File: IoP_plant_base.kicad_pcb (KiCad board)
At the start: 2 copper layers, 51.6 x 53.1 mm, 47 parts, among them IC1 HX711, J1 Conn_01x02, J2 Jack-DC, J3 Conn_01x02, J4 Conn_01x02, J5 Conn_01x03, J6 Conn_01x02, J7 Conn_01x05, Q1 BC857C, U1 NodeMCUv2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

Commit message: Started routing boost converter. TODO: footprint name fixing.
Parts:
- moved R3 57.7 mm to (114.4, 77.7)
- moved R2 57.5 mm to (115.9, 83.4)
- moved C4 52.6 mm to (114.3, 80.0), turned to 180 degrees
- moved R1 52.3 mm to (119.5, 83.2), turned to 180 degrees
- moved C3 50.1 mm to (122.8, 82.7), turned to 90 degrees
- moved C5 47.1 mm to (119.7, 74.4), turned to 270 degrees
- moved D2 43.0 mm to (124.1, 76.3), turned to 270 degrees
- moved U2 39.3 mm to (119.7, 79.0)
- moved J4 37.6 mm to (100.4, 82.3), turned to 90 degrees
- moved L1 35.5 mm to (126.2, 82.4)
- moved D1 30.4 mm to (140.1, 77.5)
- moved C2 28.1 mm to (134.9, 82.9)
- moved F1 27.3 mm to (134.8, 77.8)
- moved C1 27.2 mm to (134.9, 80.6)
- moved J3 25.5 mm to (103.9, 90.0), turned to 180 degrees
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
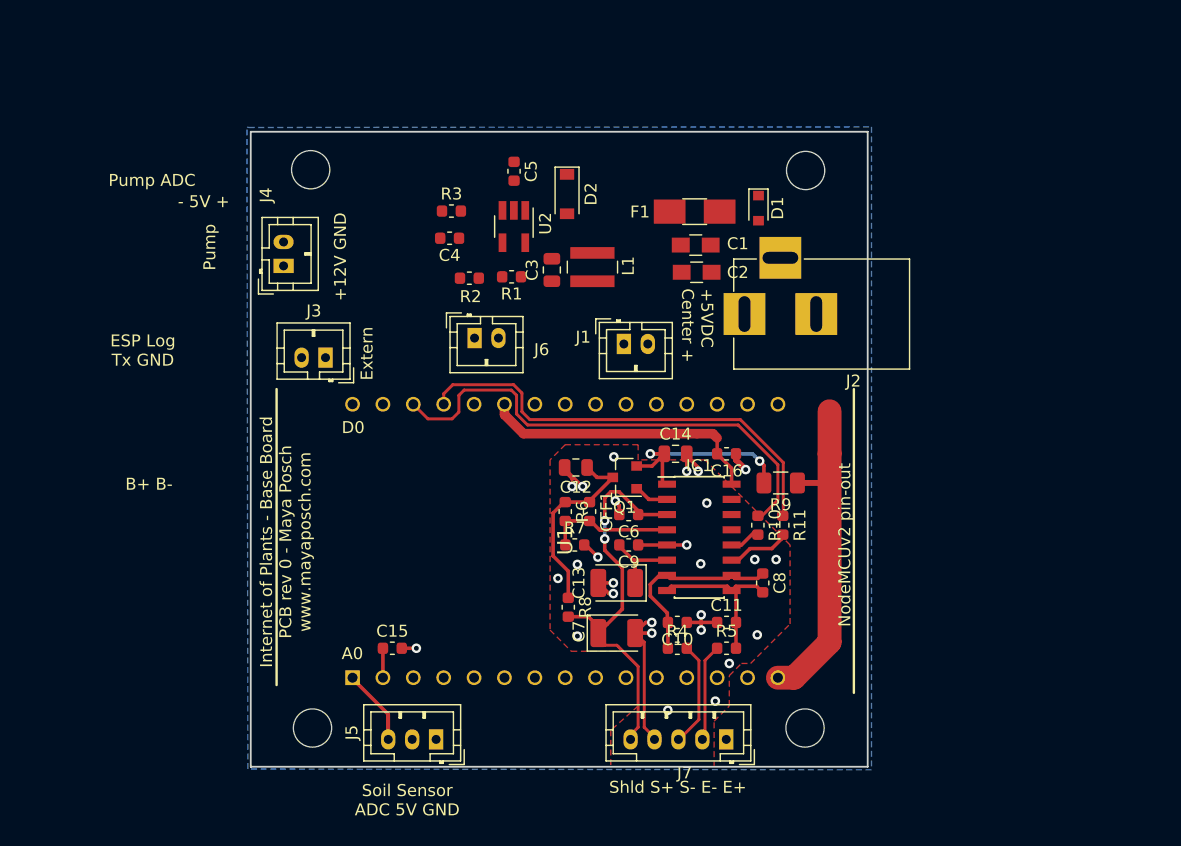
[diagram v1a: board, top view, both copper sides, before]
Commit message: Finish initial PCB routing.
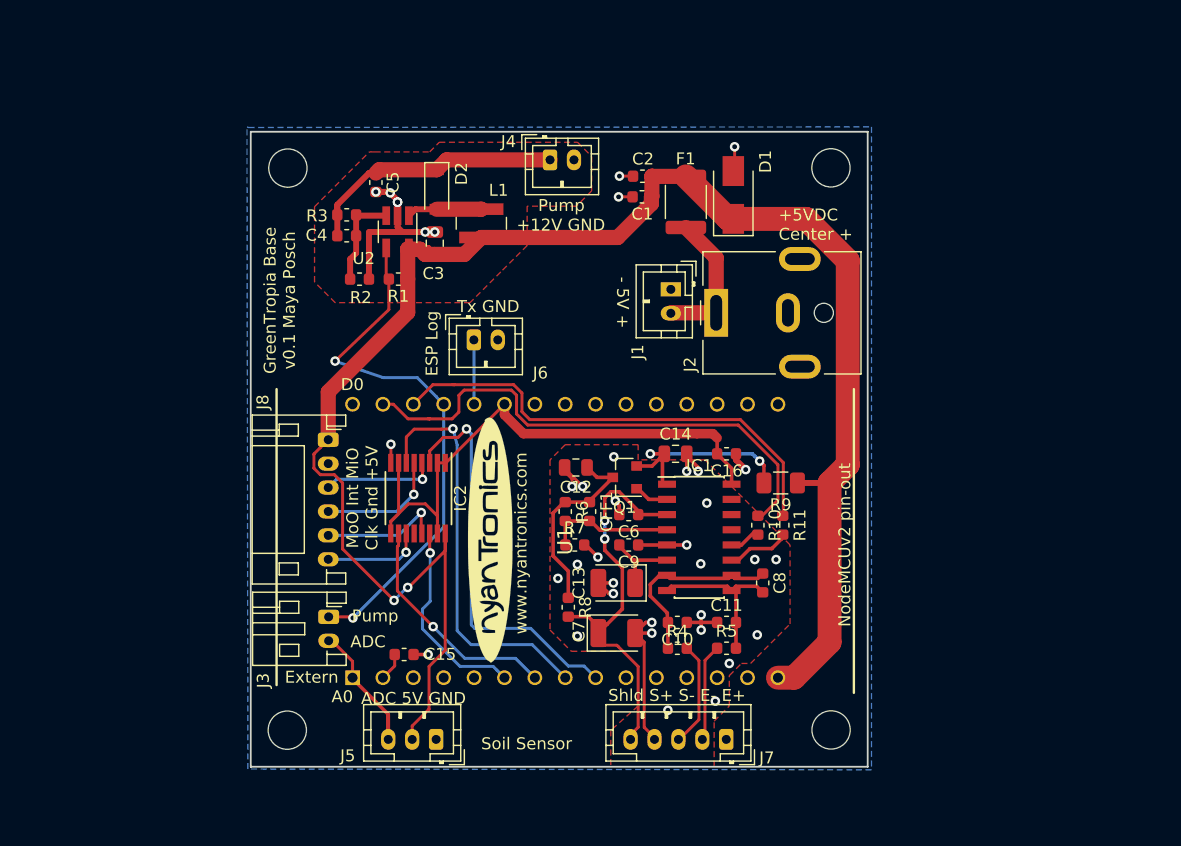
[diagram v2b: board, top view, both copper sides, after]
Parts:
- removed REF** (x4): MountingHole_3.2mm_M3_DIN965, Mounting_Holes:MountingHole_3.2mm_M3_DIN965
- added G***: LOGO, kicad_art:nyantronics_logo, F.Cu at (117.6, 105.3)
- added H1: MountingHole, MountingHole:MountingHole_3.2mm_M3_DIN965, F.Cu at (146.2, 121.1)
- added H2: MountingHole, MountingHole:MountingHole_3.2mm_M3_DIN965, F.Cu at (146.2, 74.1)
- added H3: MountingHole, MountingHole:MountingHole_3.2mm_M3_DIN965, F.Cu at (100.7, 121.1)
- added H4: MountingHole, MountingHole:MountingHole_3.2mm_M3_DIN965, F.Cu at (100.8, 74.2)
- added IC2: CD40109BPW, Package_SO:TSSOP-16_4.4x5mm_P0.65mm, F.Cu at (111.6, 101.8)
- added J8: Conn_01x06, Connector_JST:JST_PH_S6B-PH-K_1x06_P2.00mm_Horizontal, F.Cu at (104.1, 96.9)
- C1, C2: footprint Capacitors_SMD:C_0805_HandSoldering -> Capacitor_SMD:C_0603_1608Metric
- D1: footprint Diodes_SMD:D_0805 -> Diode_SMD:D_SMA
- F1: footprint Fuse_Holders_and_Fuses:Fuse_SMD1206_HandSoldering -> Fuse:Fuse_1812_4532Metric
- J2: footprint Connectors:BARREL_JACK -> Connector_BarrelJack:BarrelJack_CUI_PJ-063AH_Horizontal
- J3: footprint Connectors_JST:JST_PH_B2B-PH-K_02x2.00mm_Straight -> Connector_JST:JST_PH_S2B-PH-K_1x02_P2.00mm_Horizontal
- J4, J6: footprint Connectors_JST:JST_PH_B2B-PH-K_02x2.00mm_Straight -> Connector_JST:JST_PH_B2B-PH-K_1x02_P2.00mm_Vertical
- J5: footprint Connectors_JST:JST_PH_B3B-PH-K_03x2.00mm_Straight -> Connector_JST:JST_PH_B3B-PH-K_1x03_P2.00mm_Vertical
- J7: footprint Connectors_JST:JST_PH_B5B-PH-K_05x2.00mm_Straight -> Connector_JST:JST_PH_B5B-PH-K_1x05_P2.00mm_Vertical
- moved J4 24.0 mm to (122.7, 73.5), turned to 0 degrees
- moved J3 21.7 mm to (104.2, 111.7), turned to 270 degrees
- moved C5 11.6 mm to (108.1, 75.4)
- moved D2 10.9 mm to (113.2, 75.9)
- moved C3 10.0 mm to (113.0, 80.4)
- moved L1 9.98 mm to (116.9, 78.8)
- moved U2 9.73 mm to (109.9, 79.5)
- moved R1 9.47 mm to (110.0, 83.4)
- moved C2 9.22 mm to (130.4, 74.8), turned to 180 degrees
- moved R2 9.18 mm to (106.8, 83.4)
- moved R3 8.76 mm to (105.7, 78.1)
- moved C4 8.61 mm to (105.7, 79.8)
- moved C1 6.04 mm to (130.4, 76.6), turned to 180 degrees
- moved J1 6.02 mm to (132.8, 84.3), turned to 270 degrees
- moved D1 2.37 mm to (138.0, 76.4), turned to 90 degrees
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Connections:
- net Net-(J6-Pad1) renamed /Dbg
- U1 pad 27: SCL_CLK -> PUMP_EN
- U1 pad 28: SCL_DOUT -> SCL_CLK
- U1 pad 29: PUMP_EN -> SCL_DOUT
- U1 pad 6: Net-(U1-Pad6) -> SPI_INT
- U1 pad 7: Net-(U1-Pad7) -> SPI_MOSI
- U1 pad 8: Net-(U1-Pad8) -> SPI_MISO
- U1 pad 9: Net-(U1-Pad9) -> SPI_CLK
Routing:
- net +5VDC: track 27.5 -> 149.1 mm, vias 0 -> 2
- net PUMP_EN: track 0.00 -> 44.9 mm, vias 0 -> 2
- net SPI_MISO: track 0.00 -> 33.9 mm, vias 0 -> 1
- net SPI_CLK: track 0.00 -> 33.6 mm, vias 0 -> 1
- net +3.3V: track 23.8 -> 48.9 mm
- net +12VDC: track 0.00 -> 21.9 mm
- net GND: track 37.2 -> 58.8 mm, vias 27 -> 37
- net SPI_MOSI: track 0.00 -> 19.3 mm, vias 0 -> 1
- net SPI_INT: track 0.00 -> 16.8 mm, vias 0 -> 1
- net Net-(F1-Pad2): track 0.00 -> 12.0 mm
- net MISO_OUT: track 0.00 -> 10.4 mm, vias 0 -> 1
- net INT_OUT: track 0.00 -> 10.3 mm, vias 0 -> 1
- net CLK_OUT: track 0.00 -> 9.55 mm, vias 0 -> 1
- net MOSI_OUT: track 0.00 -> 8.33 mm, vias 0 -> 1
- net Net-(C4-Pad1): track 0.00 -> 8.13 mm
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- added copper zone on F.Cu, net (none)
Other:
- board text added: "ADC"
- board text added: "ADC 5V GND"
- board text added: "ESP Log"
- board text added: "GreenTropia Base v0.1 Maya Posch"
- board text added: "MoO Int MiO Clk Gnd +5V"
- board text added: "Soil Sensor"
- board text added: "Tx GND"
- board text added: "www.nyantronics.com"
- board text removed: "B+ B-"
- board text removed: "ESP Log Tx GND"
- board text removed: "Internet of Plants - Base Board PCB rev 0 - Maya Posch www.mayaposch.com"
- board text removed: "Pump ADC"
- board text removed: "Soil Sensor ADC 5V GND"

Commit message: PCB schematic and layout updated. More changes to actual footprints (all headers are now vertical), some BOM info added. Re-routed DCDC section. *** TODO *** rules-check everything including pinouts. Replace fiducials. Sleep.
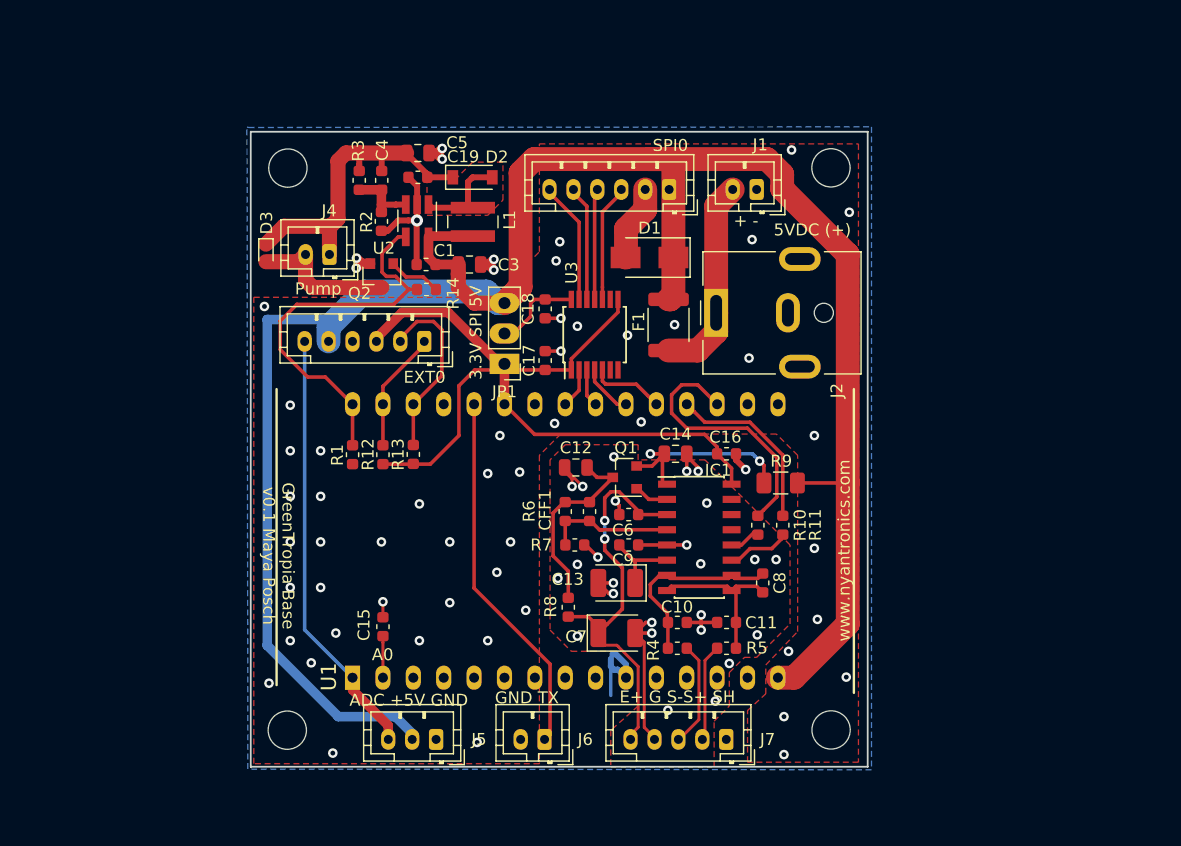
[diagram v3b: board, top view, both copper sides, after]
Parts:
- removed C2: 1uF, Capacitor_SMD:C_0603_1608Metric
- removed G***: LOGO, kicad_art:nyantronics_logo
- removed IC2: CD40109BPW, Package_SO:TSSOP-16_4.4x5mm_P0.65mm
- removed J3: Conn_01x02, Connector_JST:JST_PH_S2B-PH-K_1x02_P2.00mm_Horizontal
- removed J8: Conn_01x06, Connector_JST:JST_PH_S6B-PH-K_1x06_P2.00mm_Horizontal
- added C17: 100nF, Capacitor_SMD:C_0603_1608Metric, F.Cu at (122.3, 90.2)
- added C18: 100nF, Capacitor_SMD:C_0603_1608Metric, F.Cu at (122.3, 85.9)
- added C19: 100nF, Capacitor_SMD:C_0603_1608Metric, F.Cu at (111.6, 74.9)
- added D3: ESD5Z12T1G, Diode_SMD:D_SOD-523, F.Cu at (98.9, 81.2)
- added EXT0: Conn_01x06, Connector_JST:JST_PH_B6B-PH-K_1x06_P2.00mm_Vertical, F.Cu at (112.2, 88.6)
- added JP1: Jumper_3_Bridged12, Connector_PinHeader_2.54mm:PinHeader_1x03_P2.54mm_Vertical, F.Cu at (118.9, 90.5)
- added Q2: IRLML6244, Package_TO_SOT_SMD:SOT-23, F.Cu at (108.6, 83.1)
- added R12: 4.7k, Resistor_SMD:R_0603_1608Metric, F.Cu at (108.7, 98.1)
- added R13: 4.7k, Resistor_SMD:R_0603_1608Metric, F.Cu at (111.3, 98.1)
- added R14: 100, Resistor_SMD:R_0603_1608Metric, F.Cu at (112.3, 84.3)
- added SPI0: Conn_01x06, Connector_JST:JST_PH_B6B-PH-K_1x06_P2.00mm_Vertical, F.Cu at (132.6, 75.9)
- added U3: TXB0104PWR, Package_SO:TSSOP-14_4.4x5mm_P0.65mm, F.Cu at (126.4, 88.1)
- C5: footprint Capacitor_SMD:C_0603_1608Metric -> Capacitor_SMD:C_0805_2012Metric
- D1: value D -> 1N4004
- D2: value MBR0520 -> MBR0520L
- J1: footprint Connectors_JST:JST_PH_B2B-PH-K_02x2.00mm_Straight -> Connector_JST:JST_PH_B2B-PH-K_1x02_P2.00mm_Vertical
- R1: value 51K -> 4.7k
- moved J6 33.9 mm to (122.2, 121.9), turned to 180 degrees
- moved J4 20.1 mm to (104.2, 81.4), turned to 180 degrees
- moved C1 18.9 mm to (112.3, 82.2)
- moved R1 15.2 mm to (106.2, 98.1), turned to 270 degrees
- moved J1 11.0 mm to (140.0, 75.9), turned to 180 degrees
- moved F1 10.4 mm to (132.6, 87.3)
- moved D1 8.74 mm to (131.0, 81.6), turned to 180 degrees
- moved C4 5.48 mm to (108.6, 75.2), turned to 90 degrees
- moved R2 5.16 mm to (108.6, 78.6), turned to 270 degrees
- moved C5 4.29 mm to (111.6, 72.9), turned to 0 degrees
- moved C3 3.41 mm to (115.9, 82.2), turned to 0 degrees
- moved D2 3.16 mm to (116.2, 74.9), turned to 0 degrees
- moved R3 3.07 mm to (106.7, 75.2), turned to 270 degrees
- moved C15 2.93 mm to (108.7, 112.5), turned to 90 degrees
- moved U2 1.88 mm to (111.6, 78.6)
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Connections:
- J4 pad 2: GND -> +12VRTN
- R1 pad 1: +5VDC -> PUMP_EN
- R1 pad 2: PUMP_EN -> GND
- R10 pad 1: SCL_DOUT -> HX711_DOUT
- R11 pad 1: SCL_CLK -> HX711_SCK
- U1 pad 18: Net-(U1-Pad18) -> HX711_DOUT
- U1 pad 19: Net-(U1-Pad19) -> HX711_SCK
- U1 pad 20: Net-(U1-Pad20) -> SPI_CSN
- U1 pad 21: Net-(U1-Pad21) -> SPI_MOSI
- U1 pad 22: Net-(U1-Pad22) -> SPI_MISO
- U1 pad 23: Net-(U1-Pad23) -> SPI_CLK
- U1 pad 27: PUMP_EN -> Net-(U1-Pad27)
- U1 pad 28: SCL_CLK -> SDA
- U1 pad 29: SCL_DOUT -> SCL
- U1 pad 30: Net-(U1-Pad30) -> PUMP_EN
- U1 pad 6: SPI_INT -> Net-(U1-Pad6)
- U1 pad 7: SPI_MOSI -> Net-(U1-Pad7)
- U1 pad 8: SPI_MISO -> Net-(U1-Pad8)
- U1 pad 9: SPI_CLK -> Net-(U1-Pad9)
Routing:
- net SCL_DOUT: track 44.2 -> 0.00 mm
- net SCL_CLK: track 39.9 -> 0.00 mm
- net +5VDC: track 149.1 -> 180.8 mm, vias 2 -> 0
- net SPI_MISO: track 33.9 -> 3.17 mm, vias 1 -> 0
- net SPI_CLK: track 33.6 -> 3.35 mm, vias 1 -> 0
- net /Dbg: track 5.39 -> 30.8 mm
- net ADC: track 12.3 -> 36.2 mm
- net HX711_DOUT: track 0.00 -> 22.3 mm
- net +3.3V: track 48.9 -> 69.3 mm
- net SPI_INT: track 16.8 -> 0.00 mm, vias 1 -> 0
- net SDA: track 0.00 -> 15.3 mm
- net SPI_MOSI: track 19.3 -> 4.39 mm, vias 1 -> 0
- net HX711_SCK: track 0.00 -> 14.9 mm
- net GND: track 58.8 -> 72.5 mm, vias 37 -> 82
- net +12VRTN: track 0.00 -> 12.3 mm
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- added copper zone on F.Cu, net Net-(D2-Pad2)
- removed copper zone on F.Cu, net (none)
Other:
- board text added: "(+)"
- board text added: "+ -"
- board text added: "+12V"
- board text added: "+3.3V"
- board text added: "+5V"
- board text added: "1"
- board text added: "3.3V SPI 5V"
- board text added: "5VDC (+)"
- board text added: "ADC +5V GND"
- board text added: "CSN"
- board text added: "E+"
- board text added: "E+ G S-S+ SH"
- board text added: "GND"
- board text added: "GND TX"
- board text added: "MISO"
- board text added: "MOSI"
- board text added: "PWR"
- board text added: "RTN"
- board text added: "S+"
- board text added: "S-"
- board text added: "SCK"
- board text added: "SCL"
- board text added: "SDA"
- board text added: "SHLD"
- board text added: "SPI"
- board text added: "TX"
- board text added: "debug"
- board text added: "level"
- board text added: "link"
- board text added: "pump"
- board text added: "soil sensor"
- board text added: "strain gauge"
- board text removed: "+12V GND"
- board text removed: "+5VDC Center +"
- board text removed: "- 5V +"
- board text removed: "ADC 5V GND"
- board text removed: "D0"
- board text removed: "ESP Log"
- board text removed: "Extern"
- board text removed: "MoO Int MiO Clk Gnd +5V"
- board text removed: "NodeMCUv2 pin-out"
- board text removed: "Shld S+ S- E- E+"
- board text removed: "Soil Sensor"
- board text removed: "Tx GND"

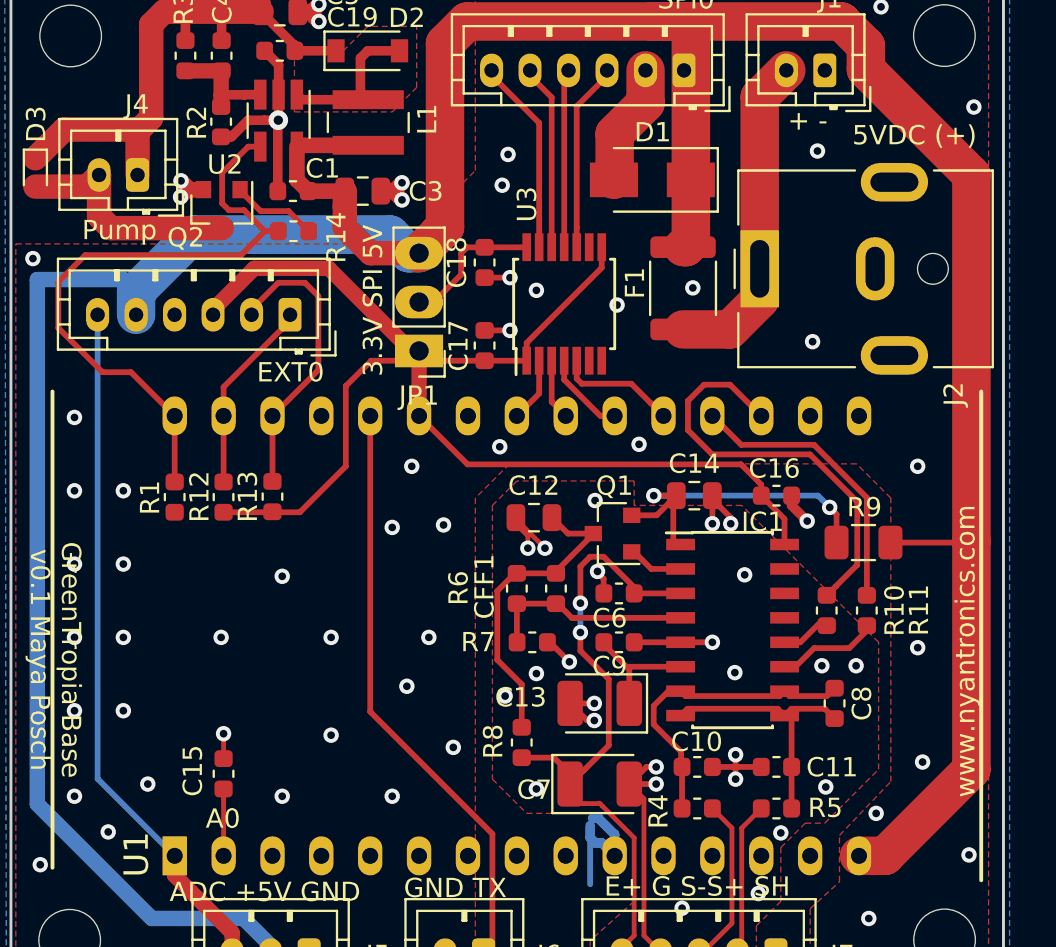
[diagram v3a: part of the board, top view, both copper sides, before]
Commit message: Generate Gerber files. Small silkscreen tweaks & clean-up.
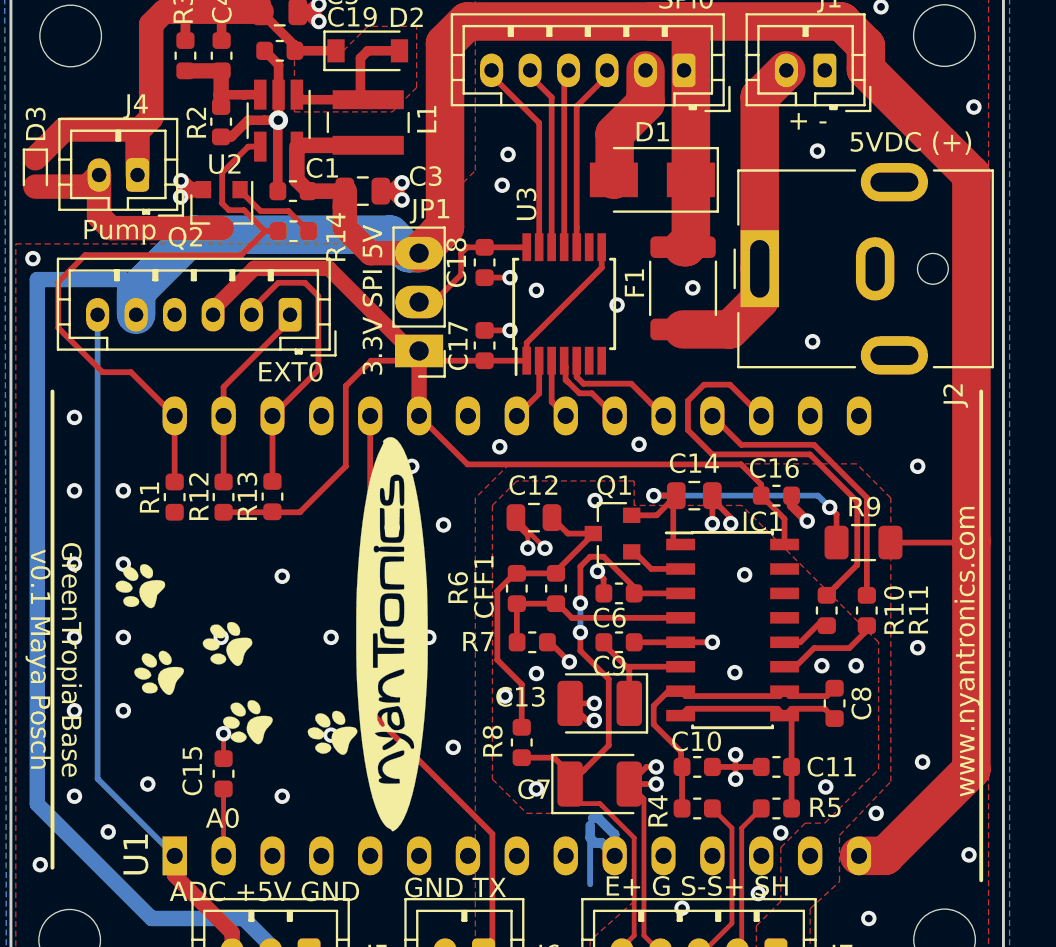
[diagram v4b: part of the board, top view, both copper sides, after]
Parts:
- added G***: LOGO, kicad_art:nyantronics_logo, F.Cu at (117.4, 105.3)
- added G***: LOGO, kicad_art:kitten_paw_prints, F.Cu at (109.4, 106.6)
